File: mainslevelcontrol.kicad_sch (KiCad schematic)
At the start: 0 parts

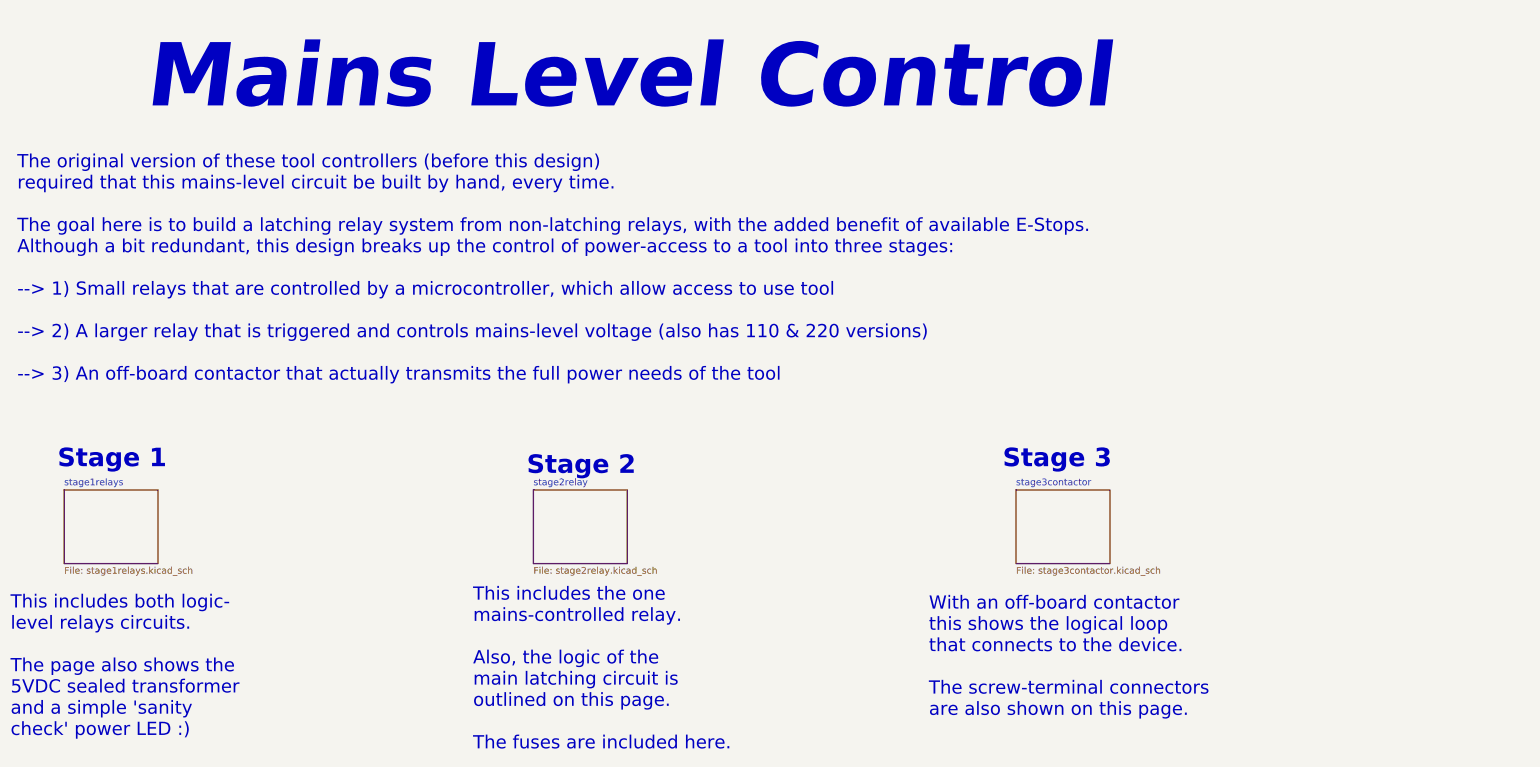
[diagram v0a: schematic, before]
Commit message: double-check mains connections, update notes
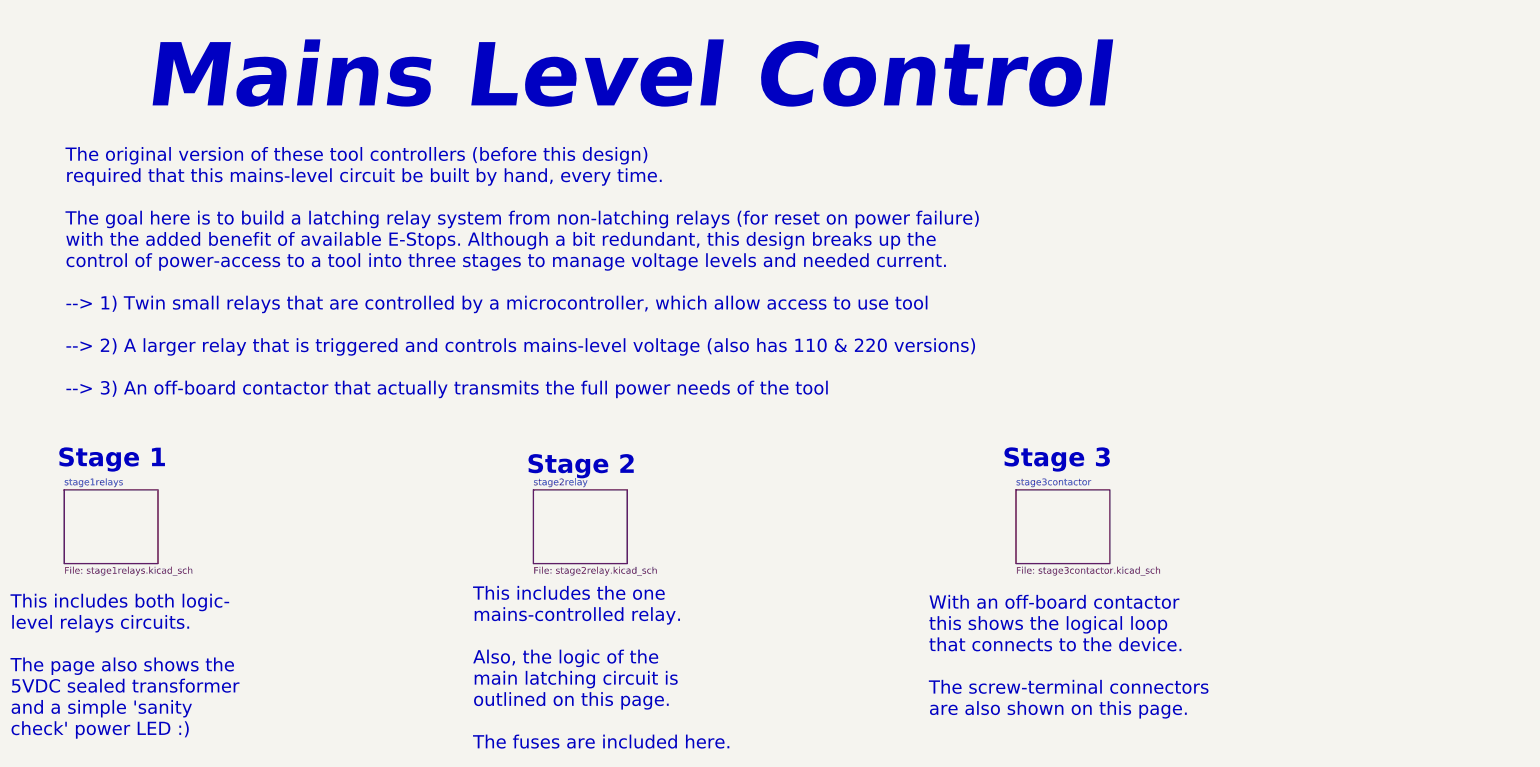
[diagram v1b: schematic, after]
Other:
- note added: "The original version of these tool controllers (before this design) required that this mains-level circuit be built by hand, every time. The goal here is to build a latching relay system from non-latching relays (for reset on power failure) with the added benefit of available E-Stops. Although a bit redundant, this design breaks up the control of power-access to a tool into three stages to manage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"
- note removed: "The original version of these tool controllers (before this design) required that this mains-level circuit be built by hand, every time. The goal here is to build a latching relay system from non-latching relays, with the added benefit of available E-Stops. Although a bit redundant, this design breaks up the control of power-access to a tool into three stages: --> 1) Small relays that are control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"
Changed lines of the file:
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@@
 		)
 	)
-	(text "The original version of these tool controllers (before this design) \nrequired that this mains-level circuit be built by hand, every time. \n\nThe goal here is to build a latching relay system from non-latching relays, with the added benefit of available E-Stops. \nAlthough a bit redundant, this design breaks up the control of power-access to a tool into three stages: \n\n--> 1) Small relays that are controlled by a microcontroller, which allow access to use tool\n\n--> 2) A larger relay that is triggered and controls mains-level voltage (also has 110 & 220 versions)\n\n--> 3) An off-board contactor that actually transmits the full power needs of the tool"
+	(text "The original version of these tool controllers (before this design) \nrequired that this mains-level circuit be built by hand, every time. \n\nThe goal here is to build a latching relay system from non-latching relays (for reset on power failure)\nwith the added benefit of available E-Stops. Although a bit redundant, this design breaks up the \ncontrol of power-access to a tool into three stages to manage voltage levels and needed current. \n\n--> 1) Twin small relays that are controlled by a microcontroller, which allow access to use tool\n\n--> 2) A larger relay that is triggered and controls mains-level voltage (also has 110 & 220 versions)\n\n--> 3) An off-board contactor that actually transmits the full power needs of the tool"
 		(exclude_from_sim no)
-		(at 24.13 100.33 0)
+		(at 33.274 103.124 0)
 		(effects
 			(font
@@
 		)
 		(instances
-			(project "mh-custom-v1.3"
+			(project "wing-combo"
 				(path "/586efc0f-7de2-49a7-ac21-ecfef2f716d6/6f44f9bb-3a88-498d-9739-be3794f35f17"
 					(page "10")
@@
 		)
 		(instances
-			(project "mh-custom-v1.3"
+			(project "wing-combo"
 				(path "/586efc0f-7de2-49a7-ac21-ecfef2f716d6/6f44f9bb-3a88-498d-9739-be3794f35f17"
 					(page "8")
@@
 		)
 		(instances
-			(project "mh-custom-v1.3"
+			(project "wing-combo"
 				(path "/586efc0f-7de2-49a7-ac21-ecfef2f716d6/6f44f9bb-3a88-498d-9739-be3794f35f17"
 					(page "9")
